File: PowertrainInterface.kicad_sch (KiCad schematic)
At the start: 0 parts

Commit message: MCU+CAN
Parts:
- added C15, C17: 0u1, Capacitor_SMD:C_0603_1608Metric, symbol Device:C
- added C16, C18, C19: 10u, Capacitor_SMD:C_1210_3225Metric, symbol Device:C
- added C20: 1n/1kV, Capacitor_SMD:C_1206_3216Metric, symbol Device:C
- added D5: PESD2CAN, Package_TO_SOT_SMD:SOT-23, symbol Device:D_TVS_Dual_AAC
- added J7: IEC61076-2_M8_B-coding_01x03_Plug_Shielded, Connector_Amphenol:Amphenol_M8S-03PMMR-SF8001, symbol Connector:IEC61076-2_M8_A-coding_01x03_Plug_Shielded
- added L3: L_Ferrite, Inductor_SMD:L_1210_3225Metric, symbol Device:L_Ferrite
- added R10: 1M, Resistor_SMD:R_1206_3216Metric, symbol Device:R
- added R11, R12: 10k, Resistor_SMD:R_0603_1608Metric, symbol Device:R
- added R8, R9: 10R, Resistor_SMD:R_0603_1608Metric, symbol Device:R
- added U4: CA-IS2062W, Package_SO:SOIC-16W_7.5x10.3mm_P1.27mm, symbol E-M-IntegratedCircuits:CA-IS2062W
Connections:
- new net: C15.1, C16.1, R11.1, U4.11 (Viso), U4.16 (Viso)
- new net: C17.1, C18.1, L3.2, U4.1 (Vcc)
- new net: R9.1, U4.12 (L)
- new net: D5.1 (A1), J7.1, R12.2, R9.2
- new net: D5.2 (A2), J7.3, R11.2, R8.2
- new net: R8.1, U4.13 (H)
- new net +3.3V: C19.1, L3.1
- new net CAN_SH: C20.2, J7.SH, R10.2
- new net GND: C17.2, C18.2, C19.2, U4.2 (GNDA), U4.8 (GNDA)
- new net GND1: C15.2, C16.2, C20.1, D5.3 (common), J7.2, R10.1, R12.1, U4.10 (GNDB), U4.15 (GNDB), U4.9 (GNDB)

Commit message: CAN interface into schematic of powertrain
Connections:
- net CAN1.TX: now reaches U4.3 (TX)
- net CAN1.RX: now reaches U4.5 (RX)
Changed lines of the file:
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@@
 		(color 0 0 0 0)
 	)
+	(bus_entry
+		(at 104.14 77.47)
+		(size 2.54 -2.54)
+		(stroke
+			(width 0)
+			(type default)
+		)
+	)
+	(bus_entry
+		(at 104.14 82.55)
+		(size 2.54 -2.54)
+		(stroke
+			(width 0)
+			(type default)
+		)
+	)
 	(wire
 		(pts
@@
 		)
 	)
+	(bus
+		(pts
+			(xy 87.63 92.71) (xy 104.14 92.71)
+		)
+		(stroke
+			(width 0)
+			(type default)
+		)
+	)
 	(wire
 		(pts
@@
 		)
 	)
+	(bus
+		(pts
+			(xy 104.14 77.47) (xy 104.14 92.71)
+		)
+		(stroke
+			(width 0)
+			(type default)
+		)
+	)
 	(wire
 		(pts
@@
 	(wire
 		(pts
+			(xy 106.68 80.01) (xy 118.11 80.01)
+		)
+		(stroke
+			(width 0)
+			(type default)
+		)
+	)
+	(wire
+		(pts
 			(xy 186.69 67.31) (xy 201.93 67.31)
 		)
@@
 			(width 0)
 			(type default)
+		)
+	)
+	(wire
+		(pts
+			(xy 106.68 74.93) (xy 118.11 74.93)
+		)
+		(stroke
+			(width 0)
+			(type default)
+		)
+	)
+	(label "{CAN1}"
+		(at 96.52 92.71 0)
+		(effects
+			(font
+				(size 1.27 1.27)
+			)
+			(justify left bottom)
+		)
+	)
+	(label "CAN1.TX"
+		(at 107.95 74.93 0)
+		(effects
+			(font
+				(size 1.27 1.27)
+			)
+			(justify left bottom)
+		)
+	)
+	(label "CAN1.RX"
+		(at 107.95 80.01 0)
+		(effects
+			(font
+				(size 1.27 1.27)
+			)
+			(justify left bottom)
 		)
 	)
@@
 		)
 	)
+	(hierarchical_label "{CAN1}"
+		(shape bidirectional)
+		(at 87.63 92.71 180)
+		(effects
+			(font
+				(size 1.27 1.27)
+			)
+			(justify right)
+		)
+	)

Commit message: Integration of changes into prewious style of schematic
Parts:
- added C60, C61, C62, C63, C94, C95: 100nF, symbol Device:C
- added D16, D17, D18, D19: 1N4148W, PCM_JLCPCB:D_SOD-123, symbol PCM_JLCPCB-Diodes:Switching,1N4148W
- added D31, D32: BAT54S_C7420333, PCM_JLCPCB:SOT-23-3_L2.9-W1.3-P1.90-LS2.4-BR, symbol PCM_JLCPCB-Diode-Packages:Schottky, BAT54S_C7420333
- added J19, J20: (no value), symbol higo:Z609BM_C_04_00_0000
- added R113, R115, R48, R51, R55, R56: 10kΩ, PCM_JLCPCB:R_0805, symbol PCM_JLCPCB-Resistors:0805,10kΩ
- added R114, R126: 15kΩ, PCM_JLCPCB:R_0805, symbol PCM_JLCPCB-Resistors:0805,15kΩ
- added R47, R50, R57, R58: 4.7kΩ, PCM_JLCPCB:R_0805, symbol PCM_JLCPCB-Resistors:0805,4.7kΩ
- added R49, R52, R53, R54: 20kΩ, PCM_JLCPCB:R_0805, symbol PCM_JLCPCB-Resistors:0805,20kΩ
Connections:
- net +3.3V: now also D16.1, D17.1, D18.1, D19.1, D31.2 (K2), D32.2 (K2)
- net GND: now also C60.2, C61.2, C62.2, C63.2, C94.2, C95.2, D31.1 (K1), D32.1 (K1), J19.2, J20.2, R114.2, R126.2, R49.2, R52.2, R53.2, R54.2
- new net: J19.4, R47.2, R48.1
- new net: J20.3, R56.1, R58.2
- new net: J20.4, R55.1, R57.2
- new net: J20.5, R115.1
- new net: J19.3, R50.2, R51.1
- new net: J19.5, R113.1
- new net +12V: J19.1, J20.1
- new net +5V: R47.1, R50.1, R57.1, R58.1
- new net AUX_AN: C95.1, D32.3 (A), R115.2, R126.1
- new net AUX_PAS_A: C62.1, D18.2, R53.1, R55.2
- new net AUX_PAS_B: C63.1, D19.2, R54.1, R56.2
- new net TORQUE_AN: C94.1, D31.3 (A), R113.2, R114.1
- new net TORQUE_PAS_A: C60.1, D16.2, R48.2, R49.1
- new net TORQUE_PAS_B: C61.1, D17.2, R51.2, R52.1
- no-connect marks 0 -> 2
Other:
- note added: "5V*15k/25k = 3V"
- note added: "DNP if pas have the pull up"
- note added: "Rth = R13//(R14) = 6 k C = 1 / (2*pi × 200Hz × Rth) = 100nF"
- note added: "Rth = R3//(R2+R1) = 8.4 k C = 1 / (2*pi × 200Hz × Rth) = 100nF"
- note added: "V_MCUmax = Vccmax * R3/(R1+R2+R2)=3V4 @ 6V for Vccmax V_MCUmin = Vccmin * R3/(R1+R2+R2)=2.3V @ 4V for Vccmin"
- note added: "aux"
- note added: "torque"
- moved on the sheet: C15, C16, C17, C18, C19, C20, D5, J7, L3, R10, R11, R12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

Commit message: I/O Schematic rebuild from DRAFT by Nathann
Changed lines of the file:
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@@
 	(text "torque"
 		(exclude_from_sim no)
-		(at 136.144 128.524 0)
+		(at 123.444 150.622 0)
 		(effects
 			(font
@@
 	(text "aux"
 		(exclude_from_sim no)
-		(at 255.778 129.032 0)
+		(at 245.872 151.892 0)
 		(effects
 			(font

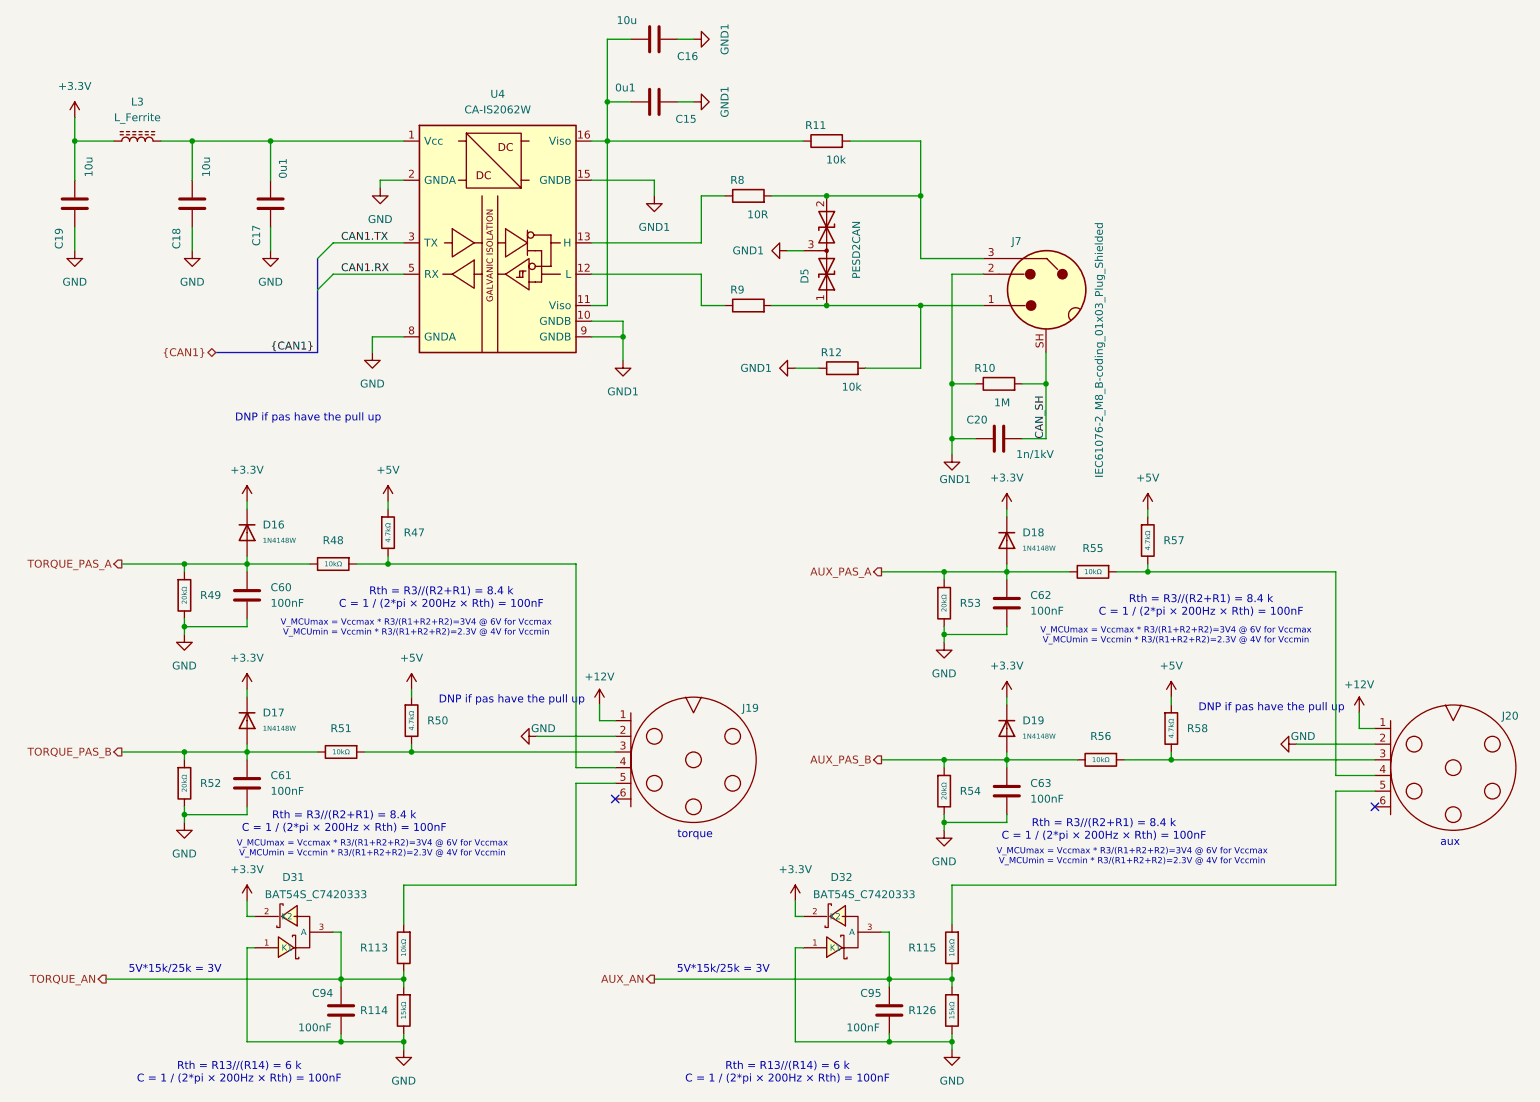
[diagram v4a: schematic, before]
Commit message: EMI/EMC meassures implementation + VCU panel interface block
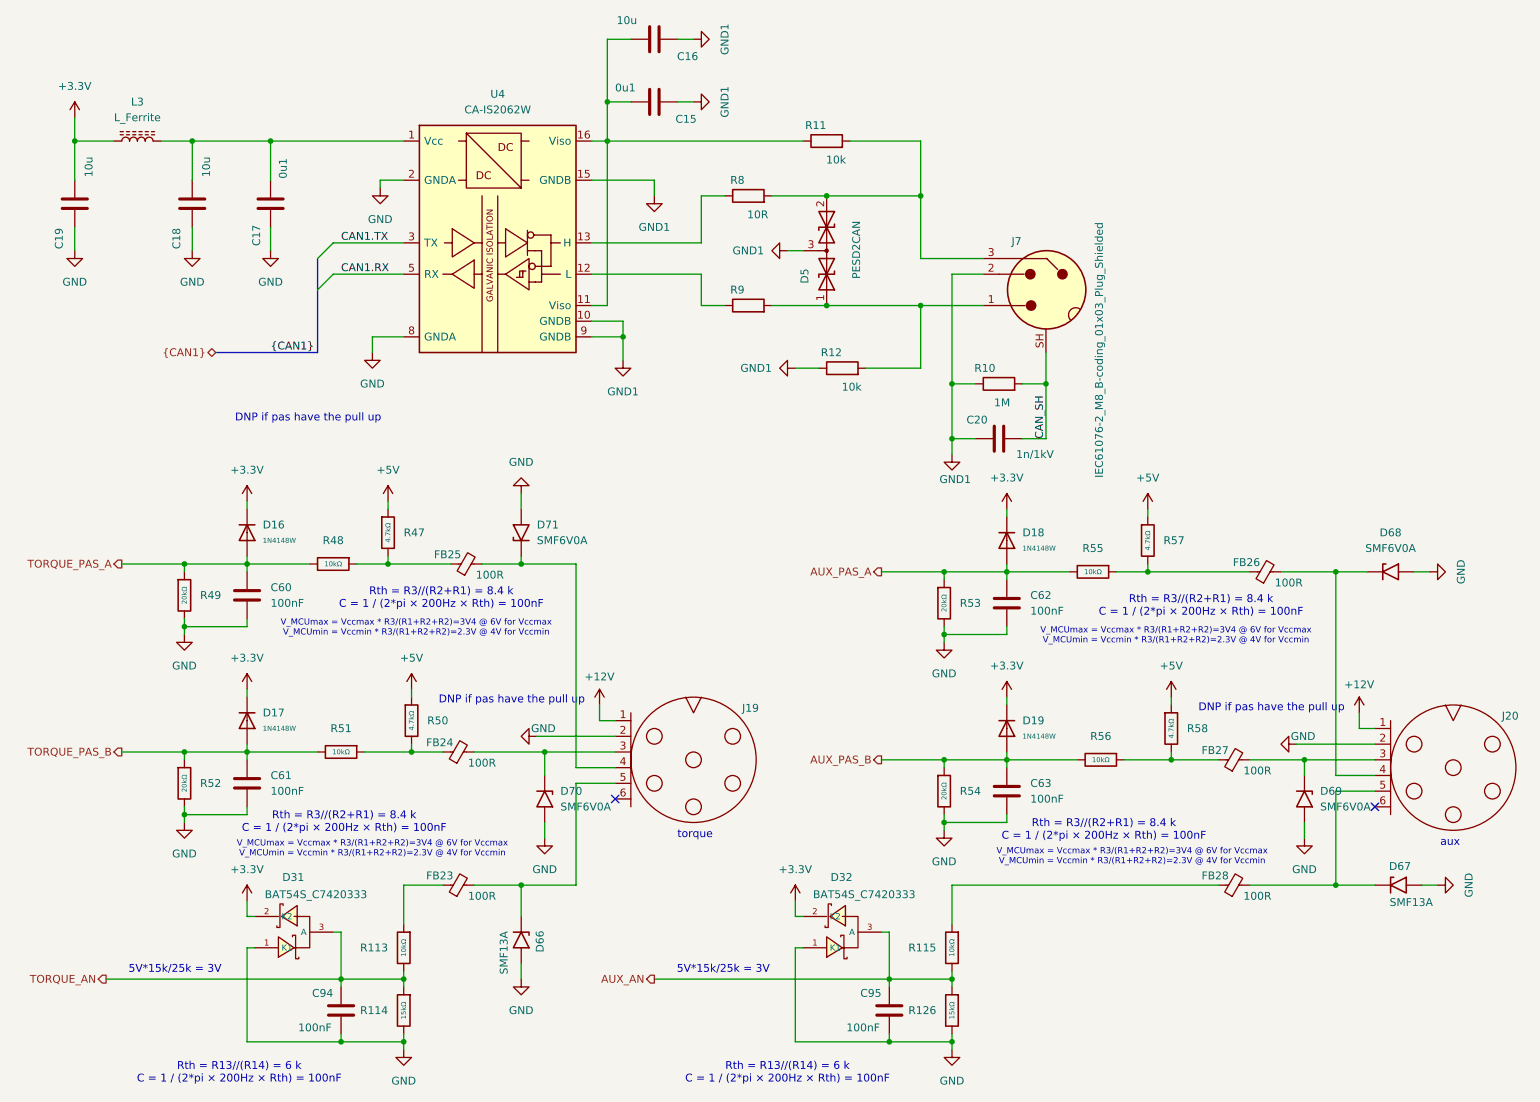
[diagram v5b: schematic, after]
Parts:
- added D66, D67: SMF13A, Diode_SMD:D_SMF, symbol VELION_VCU_Library:SMF13A
- added D68, D69, D70, D71: SMF6V0A, Diode_SMD:D_SMF, symbol VELION_VCU_Library:SMF6V0A
- added FB23, FB24, FB25, FB26, FB27, FB28: 100R, Inductor_SMD:L_0603_1608Metric, symbol VELION_VCU_Library:FerriteBead_Small
- C15, C16, C17, C18, C19, C20: symbol Device:C -> VELION_VCU_Library:C
- C60, C61, C62, C63, C94, C95: footprint (none) -> Capacitor_SMD:C_0603_1608Metric; symbol Device:C -> VELION_VCU_Library:C
- D16, D17, D18, D19: footprint PCM_JLCPCB:D_SOD-123 -> Diode_SMD:D_SOD-123; symbol PCM_JLCPCB-Diodes:Switching,1N4148W -> VELION_VCU_Library:Switching,1N4148W
- D31, D32: footprint PCM_JLCPCB:SOT-23-3_L2.9-W1.3-P1.90-LS2.4-BR -> Package_TO_SOT_SMD:SOT-23-3; symbol PCM_JLCPCB-Diode-Packages:Schottky, BAT54S_C7420333 -> VELION_VCU_Library:Schottky, BAT54S_C7420333
- D5: symbol Device:D_TVS_Dual_AAC -> VELION_VCU_Library:D_TVS_Dual_AAC
- J19, J20: symbol higo:Z609BM_C_04_00_0000 -> VELION_VCU_Library:Z609BM_C_04_00_0000
- J7: symbol Connector:IEC61076-2_M8_A-coding_01x03_Plug_Shielded -> VELION_VCU_Library:IEC61076-2_M8_A-coding_01x03_Plug_Shielded
- L3: symbol Device:L_Ferrite -> VELION_VCU_Library:L_Ferrite
- R10, R11, R12, R8, R9: symbol Device:R -> VELION_VCU_Library:R
- R113, R115, R48, R51, R55, R56: footprint PCM_JLCPCB:R_0805 -> Resistor_SMD:R_0805_2012Metric; symbol PCM_JLCPCB-Resistors:0805,10kΩ -> VELION_VCU_Library:0805,10kΩ
- R114, R126: footprint PCM_JLCPCB:R_0805 -> Resistor_SMD:R_0805_2012Metric; symbol PCM_JLCPCB-Resistors:0805,15kΩ -> VELION_VCU_Library:0805,15kΩ
- R47, R50, R57, R58: footprint PCM_JLCPCB:R_0805 -> Resistor_SMD:R_0805_2012Metric; symbol PCM_JLCPCB-Resistors:0805,4.7kΩ -> VELION_VCU_Library:0805,4.7kΩ
- R49, R52, R53, R54: footprint PCM_JLCPCB:R_0805 -> Resistor_SMD:R_0805_2012Metric; symbol PCM_JLCPCB-Resistors:0805,20kΩ -> VELION_VCU_Library:0805,20kΩ
- U4: symbol E-M-IntegratedCircuits:CA-IS2062W -> VELION_VCU_Library:CA-IS2062W
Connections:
- net GND: now also D66.2 (A2), D67.2 (A2), D68.2 (A2), D69.2 (A2), D70.2 (A2), D71.2 (A2)
- net at R47.2, R48.1: now also FB25.1; no longer J19.4
- net at R56.1, R58.2: now also FB27.1; no longer J20.3
- net at R55.1, R57.2: now also FB26.1; no longer J20.4
- net at J20.5: now also D67.1 (A1), FB28.2; no longer R115.1
- net at R50.2, R51.1: now also FB24.1; no longer J19.3
- net at J19.5: now also D66.1 (A1), FB23.2; no longer R113.1
- new net: D69.1 (A1), FB27.2, J20.3
- new net: D71.1 (A1), FB25.2, J19.4
- new net: D68.1 (A1), FB26.2, J20.4
- new net: FB28.1, R115.1
- new net: FB23.1, R113.1
- new net: D70.1 (A1), FB24.2, J19.3
